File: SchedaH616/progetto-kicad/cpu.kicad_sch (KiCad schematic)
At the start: 115 parts, among them J301 UART2 debug, SW301 RESET, SW302 RECOVERY, U301 RK3568, U302 TPD4E05U06DQA, U303 TPD4E05U06DQA, U304 TPD4E05U06DQA, U305 TPD4E05U06DQA, U306 TPD4E05U06DQA, U307 TPD4E05U06DQA, Y301 24MHz

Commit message: SchedaH616: passivi 0603, microSD sul bottom, USB-C affiancate
- passivi 0603 di default; 0201/0402 solo per il disaccoppiamento sotto RK3568 e DDR4,
  le serie RGMII/clock/USB, DDR_RZQ, ZQ e VREF della DDR4
  (C: 29x0201, 31x0402, 133x0603; R: 24x0402, 133x0603)
- microSD J401 sul bottom, apertura sul bordo sinistro
- USB-C host J801 e OTG/alimentazione J104 affiancate sul bordo basso, con ESD,
  TPS2553, TPS2121, FUSB302B e SY6280 accanto
- 387 componenti sul top, 52 sul bottom; ERC 0, parita' 0, DRC 0 (solo collegamenti)

Co-Authored-By: Claude Opus 5.5 (1M context) <noreply@anthropic.com>
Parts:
- C301, C302, C303, C304: footprint Capacitor_SMD:C_0402_1005Metric -> Capacitor_SMD:C_0603_1608Metric
- R301, R302, R303, R304, R305, R306, R307, R308, R309, R310, R311, R312, R313, R317, R318, R319, R320, R321, R322, R323, R324, R325, R326, R327, R328, R329, R330, R331, R332, R333, R334, R335, R336, R337, R338, R339: footprint Resistor_SMD:R_0402_1005Metric -> Resistor_SMD:R_0603_1608Metric

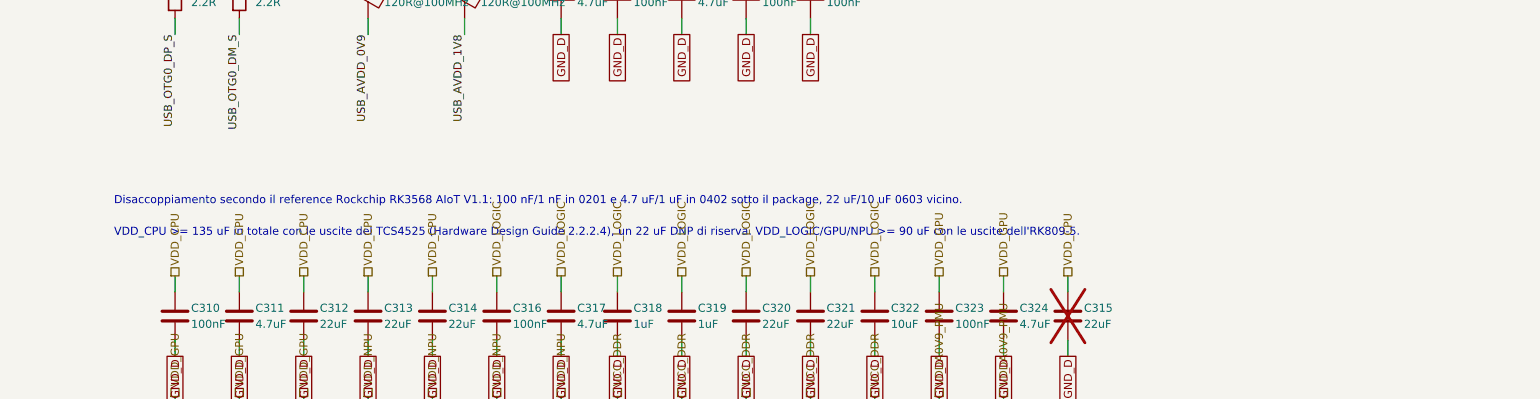
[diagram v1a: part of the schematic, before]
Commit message: SchedaH616: niente 0201, disaccoppiamento 0402 sotto le BGA
- i 29 condensatori 0201 del RK3568 diventano 0402 (stessi valori): minimo 0402 per i passivi
- disaccoppiamento di RK3568 (C305-C363) e DDR4 (C404-C418) sempre ancorato al suo package:
  59/59 sotto il RK3568 e 15/15 sotto la DDR4, sul bottom (prima 23 finivano sul top vicino alla PMIC)
- 364 componenti sul top, 75 sul bottom (74 condensatori + microSD); scheda sempre 70 x 90
- ERC 0, parita' 0, DRC 0 (solo collegamenti da fare)

Co-Authored-By: Claude Opus 5.5 (1M context) <noreply@anthropic.com>
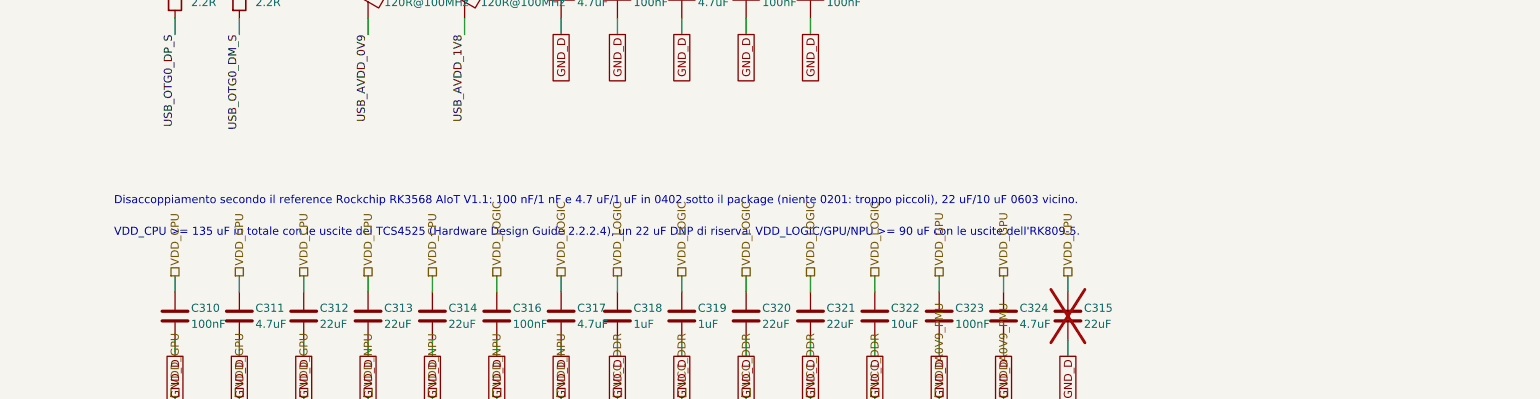
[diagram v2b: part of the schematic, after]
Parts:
- C306, C308, C309, C310, C316, C323, C328, C332, C333, C338, C340, C342, C344, C346, C347, C348, C349, C350, C351, C353, C354, C355, C356, C357, C358, C359, C360, C362, C363: footprint Capacitor_SMD:C_0201_0603Metric -> Capacitor_SMD:C_0402_1005Metric
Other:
- note added: "Disaccoppiamento secondo il reference Rockchip RK3568 AIoT V1.1: 100 nF/1 nF e 4.7 uF/1 uF in 0402 sotto il package (niente 0201: troppo piccoli), 22 uF/10 uF 0603 vicino."
- note removed: "Disaccoppiamento secondo il reference Rockchip RK3568 AIoT V1.1: 100 nF/1 nF in 0201 e 4.7 uF/1 uF in 0402 sotto il package, 22 uF/10 uF 0603 vicino."
